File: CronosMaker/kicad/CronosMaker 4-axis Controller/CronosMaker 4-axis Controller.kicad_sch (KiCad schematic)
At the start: 42 parts, among them J1 UART, J10 POW, J11 PWM, J12 LSR PWM, J2 Ctrl, J3 ISP, J4 DBG, J5 A, J6 IO, J7 Conn_01x02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

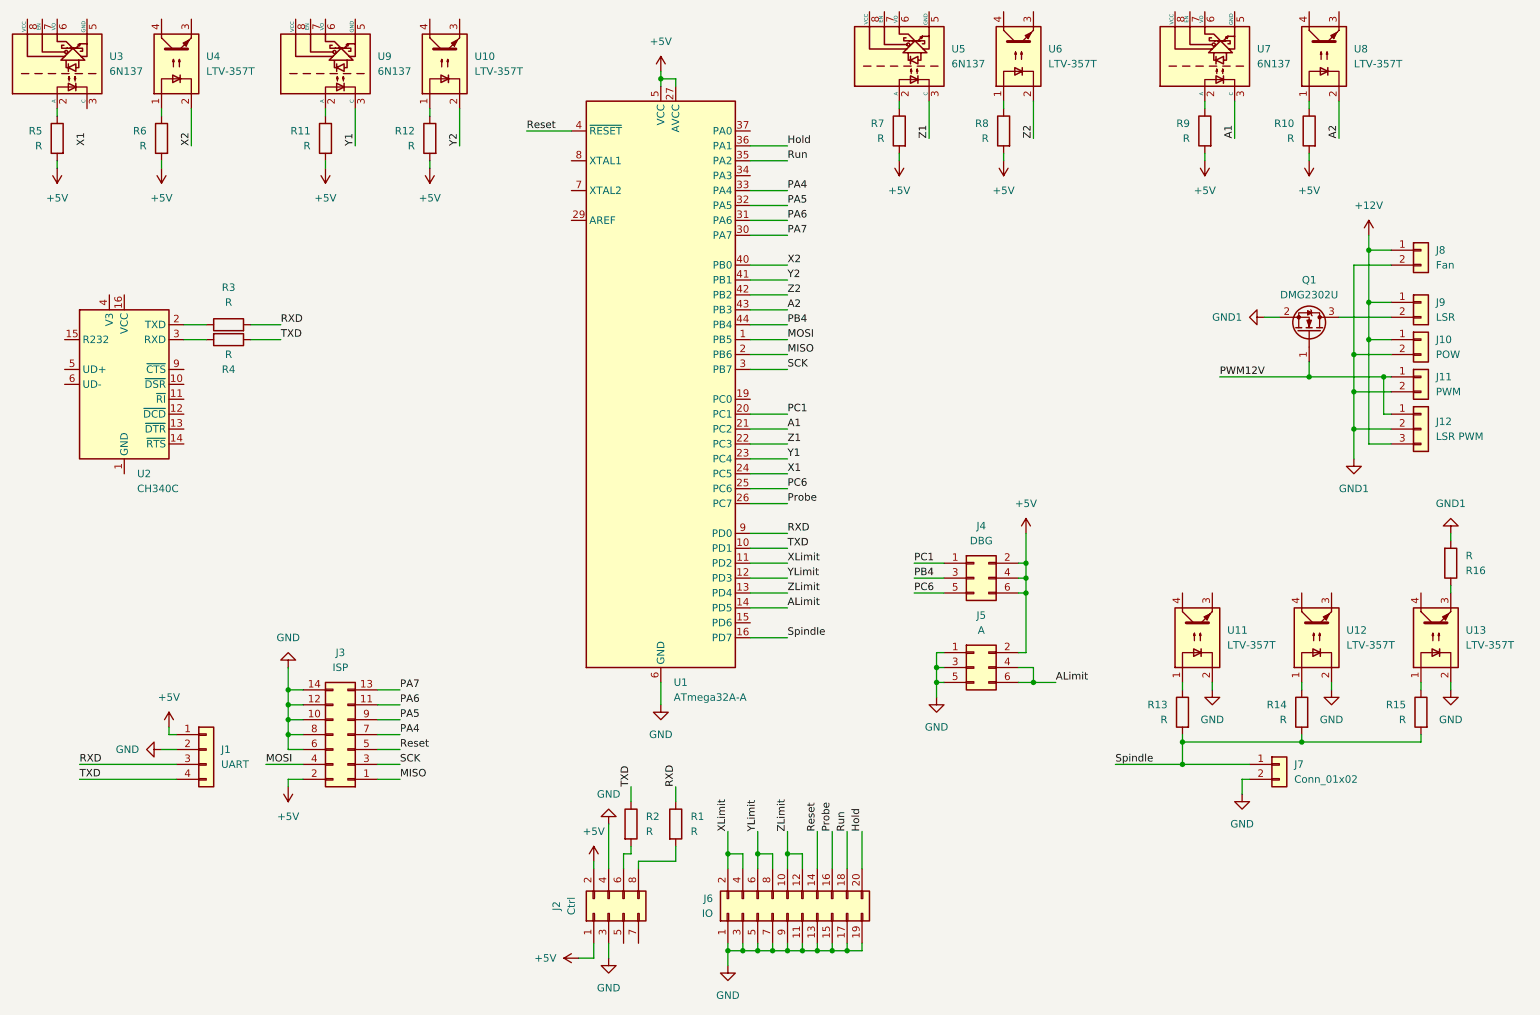
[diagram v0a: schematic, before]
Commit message: Updated CNC board schematics anf firmware note
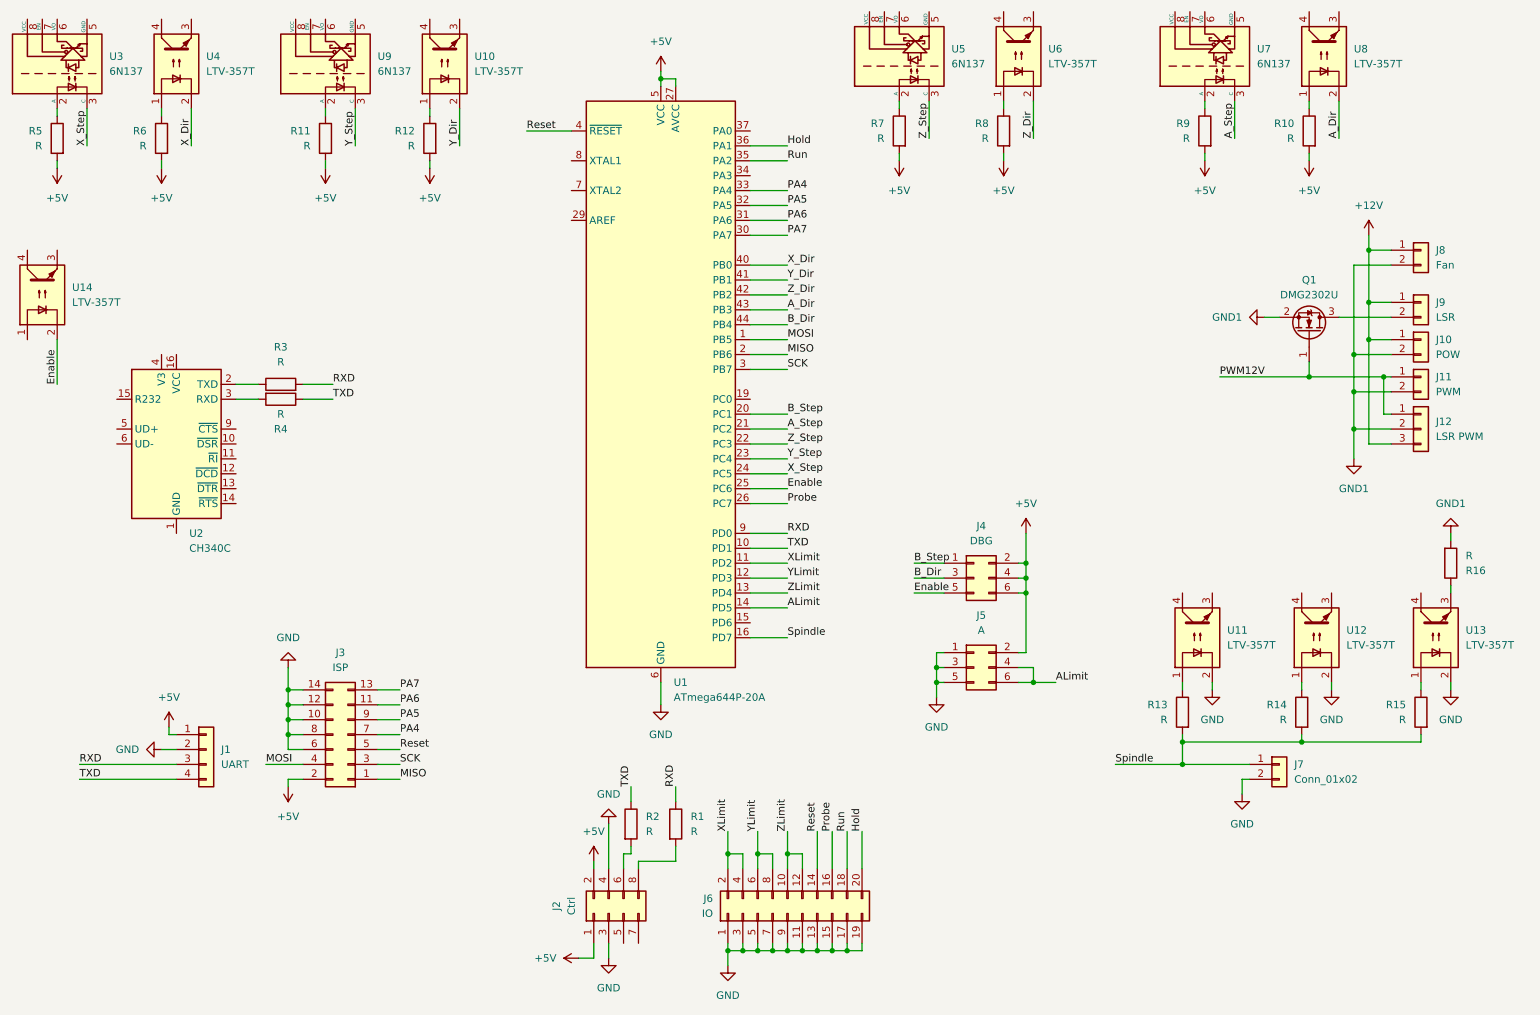
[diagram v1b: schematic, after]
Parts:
- removed U1: ATmega32A-A, Package_QFP:TQFP-44_10x10mm_P0.8mm, symbol MCU_Microchip_ATmega:ATmega32A-A
- added U1: ATmega644P-20A, Package_QFP:TQFP-44_10x10mm_P0.8mm, symbol MCU_Microchip_ATmega:ATmega644P-20A
- added U14: LTV-357T, Package_SO:SO-4_4.4x3.6mm_P2.54mm, symbol Isolator:LTV-357T
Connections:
- net +5V: now also U1.17 (VCC), U1.27 (AVCC), U1.38 (VCC), U1.5 (VCC)
- net ALimit: now also U1.14 (PD5)
- net GND: now also U1.18 (GND), U1.28 (GND), U1.39 (GND), U1.6 (GND)
- net Hold: now also U1.36 (PA1)
- net MISO: now also U1.2 (PB6)
- net MOSI: now also U1.1 (PB5)
- net PA4: now also U1.33 (PA4)
- net PA5: now also U1.32 (PA5)
- net PA6: now also U1.31 (PA6)
- net PA7: now also U1.30 (PA7)
- net Probe: now also U1.26 (PC7)
- net RXD: now also U1.9 (PD0)
- net Reset: now also U1.4 (~{RESET})
- net Run: now also U1.35 (PA2)
- net SCK: now also U1.3 (PB7)
- net Spindle: now also U1.16 (PD7)
- net TXD: now also U1.10 (PD1)
- net XLimit: now also U1.11 (PD2)
- net YLimit: now also U1.12 (PD3)
- net ZLimit: now also U1.13 (PD4)
- net X_Step: now reaches U3.3 (C)
- net X_Step: now also U1.24 (PC5)
- net A1 renamed A_Step
- net A_Step: now also U1.21 (PC2)
- net A2 renamed A_Dir
- net A_Dir: now also U1.43 (PB3)
- net PB4 renamed B_Dir
- net B_Dir: now also U1.44 (PB4)
- net PC1 renamed B_Step
- net B_Step: now also U1.20 (PC1)
- net PC6 renamed Enable
- net Enable: now also U1.25 (PC6), U14.2
- net X2 renamed X_Dir
- net X_Dir: now also U1.40 (PB0)
- net Y1 renamed Y_Step
- net Y_Step: now also U1.23 (PC4)
- net Y2 renamed Y_Dir
- net Y_Dir: now also U1.41 (PB1)
- net Z1 renamed Z_Step
- net Z_Step: now also U1.22 (PC3)
- net Z2 renamed Z_Dir
- net Z_Dir: now also U1.42 (PB2)
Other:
- moved on the sheet: R3, R4, U2

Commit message: Assign control pins to aux pin header
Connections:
- net PA4 renamed Door
- net PA5 renamed Spindle_Dir
- net PA6 renamed Coolant_Flood
- net PA7 renamed Coolant_Mist
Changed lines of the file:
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@@
     (effects (font (size 1.27 1.27)) (justify left bottom))
   )
-  (label "PA4" (at 152.4 54.61 0) (fields_autoplaced)
+  (label "Door" (at 152.4 54.61 0) (fields_autoplaced)
     (effects (font (size 1.27 1.27)) (justify left bottom))
   )
@@
     (effects (font (size 1.27 1.27)) (justify left bottom))
   )
-  (label "PA6" (at 86.36 142.24 0) (fields_autoplaced)
+  (label "Coolant_Flood" (at 86.36 142.24 0) (fields_autoplaced)
     (effects (font (size 1.27 1.27)) (justify left bottom))
   )
@@
     (effects (font (size 1.27 1.27)) (justify left bottom))
   )
-  (label "PA5" (at 152.4 57.15 0) (fields_autoplaced)
+  (label "Spindle_Dir" (at 152.4 57.15 0) (fields_autoplaced)
     (effects (font (size 1.27 1.27)) (justify left bottom))
   )
@@
     (effects (font (size 1.27 1.27)) (justify left bottom))
   )
-  (label "PA6" (at 152.4 59.69 0) (fields_autoplaced)
+  (label "Coolant_Flood" (at 152.4 59.69 0) (fields_autoplaced)
     (effects (font (size 1.27 1.27)) (justify left bottom))
   )
@@
     (effects (font (size 1.27 1.27)) (justify left bottom))
   )
-  (label "PA7" (at 152.4 62.23 0) (fields_autoplaced)
+  (label "Coolant_Mist" (at 152.4 62.23 0) (fields_autoplaced)
     (effects (font (size 1.27 1.27)) (justify left bottom))
   )
-  (label "PA5" (at 86.36 144.78 0) (fields_autoplaced)
+  (label "Spindle_Dir" (at 86.36 144.78 0) (fields_autoplaced)
     (effects (font (size 1.27 1.27)) (justify left bottom))
   )
@@
     (effects (font (size 1.27 1.27)) (justify left bottom))
   )
-  (label "PA4" (at 86.36 147.32 0) (fields_autoplaced)
+  (label "Door" (at 86.36 147.32 0) (fields_autoplaced)
     (effects (font (size 1.27 1.27)) (justify left bottom))
   )
@@
     (effects (font (size 1.27 1.27)) (justify left bottom))
   )
-  (label "PA7" (at 86.36 139.7 0) (fields_autoplaced)
+  (label "Coolant_Mist" (at 86.36 139.7 0) (fields_autoplaced)
     (effects (font (size 1.27 1.27)) (justify left bottom))
   )
